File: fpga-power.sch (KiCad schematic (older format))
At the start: 17 parts, among them U1 XC7K70T-FBG484

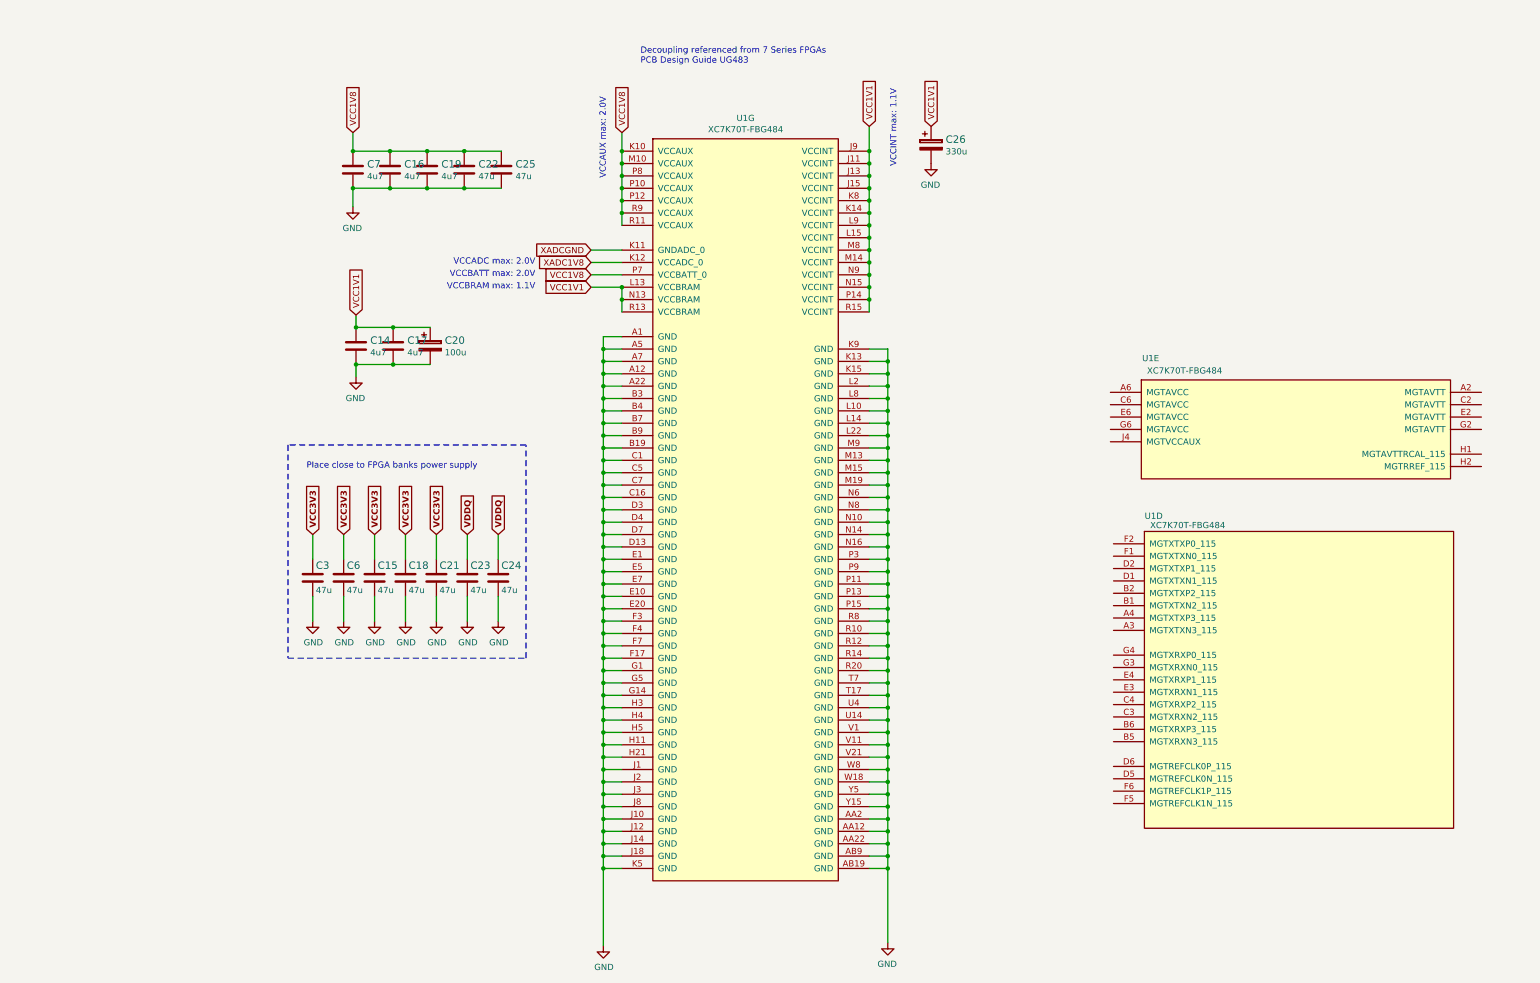
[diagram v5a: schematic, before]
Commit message: Update block descriptions
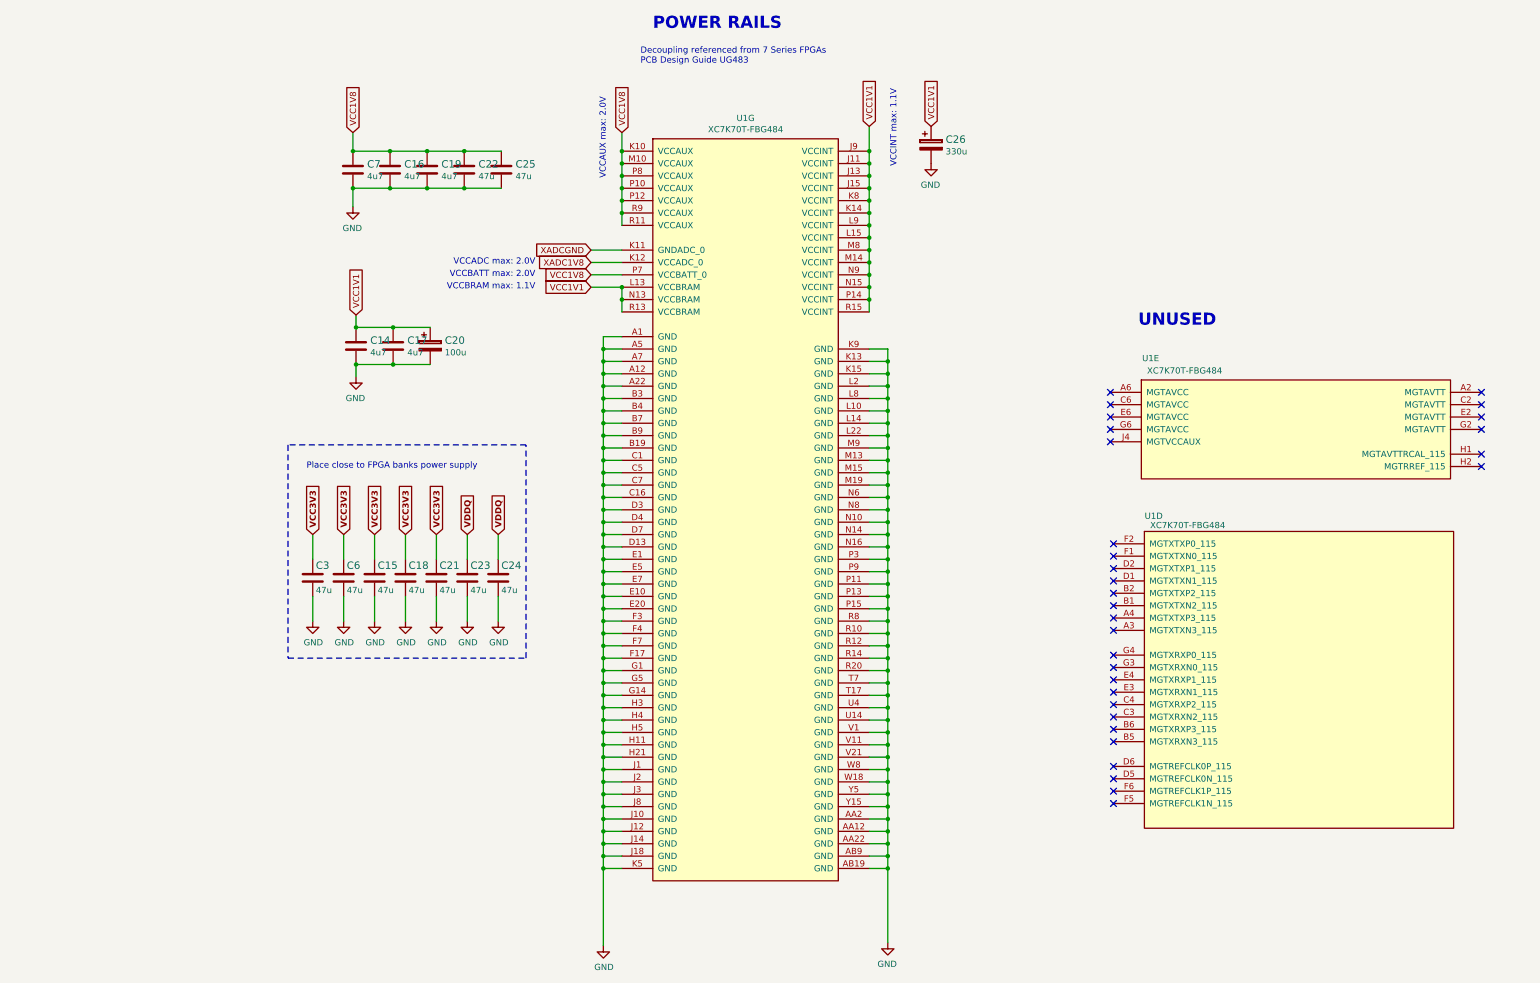
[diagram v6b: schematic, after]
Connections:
- no-connect marks 0 -> 31
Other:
- note added: "POWER RAILS"
- note added: "UNUSED"
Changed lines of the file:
@@
 	1    0    0    -1
 $EndComp
+NoConn ~ 11475 4375
+NoConn ~ 11475 4475
+NoConn ~ 11475 4575
+NoConn ~ 11475 4675
+NoConn ~ 11475 4775
+NoConn ~ 14475 4975
+NoConn ~ 14475 4875
+NoConn ~ 14475 4675
+NoConn ~ 14475 4575
+NoConn ~ 14475 4475
+NoConn ~ 14475 4375
+NoConn ~ 11500 5600
+NoConn ~ 11500 5700
+NoConn ~ 11500 5800
+NoConn ~ 11500 5900
+NoConn ~ 11500 6000
+NoConn ~ 11500 6100
+NoConn ~ 11500 6200
+NoConn ~ 11500 6300
+NoConn ~ 11500 6500
+NoConn ~ 11500 6600
+NoConn ~ 11500 6700
+NoConn ~ 11500 6800
+NoConn ~ 11500 6900
+NoConn ~ 11500 7000
+NoConn ~ 11500 7100
+NoConn ~ 11500 7200
+NoConn ~ 11500 7400
+NoConn ~ 11500 7500
+NoConn ~ 11500 7600
+NoConn ~ 11500 7700
+Text Notes 11700 3850 0    98   ~ 20
+UNUSED
+Text Notes 7775 1450 0    98   ~ 20
+POWER RAILS
 $EndSCHEMATC

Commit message: Add decoupling capacitors
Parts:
- added C? (x27): C_100n_0201, antmicro-footprints:0201-res, symbol antmicroCapacitorsmisc:C_100n_0201
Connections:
- net labels removed: XADC1V8, XADCGND
- wire segments 231 -> 288
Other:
- moved on the sheet: C14, C16, C17, C19, C20, C22, C25, C26, C7

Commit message: Place and route decoupling capacitors
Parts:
- removed C?: C_100n_0201, antmicro-footprints:0201-res, symbol antmicroCapacitorsmisc:C_100n_0201
- gave numbers to parts that had none: 26
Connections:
- wire segments 288 -> 286
